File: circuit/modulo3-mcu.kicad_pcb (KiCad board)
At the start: 2 copper layers, 87 x 52 mm, 49 parts, among them Q1 BS250, Q2 BS170, U1 74LVC2G32DC, U10 PWR_CONN, U11 FOOTSWITCH, U13 LM1117 3V3, U2 AVR64DA64, U3 SN74LVC1G17, U4 UPDI, U5 TOUCHSCREEN_240x320, U6 FV1_CONN, U7 DBG_UART, U8 AMPCTRL, Y1 32768Hz

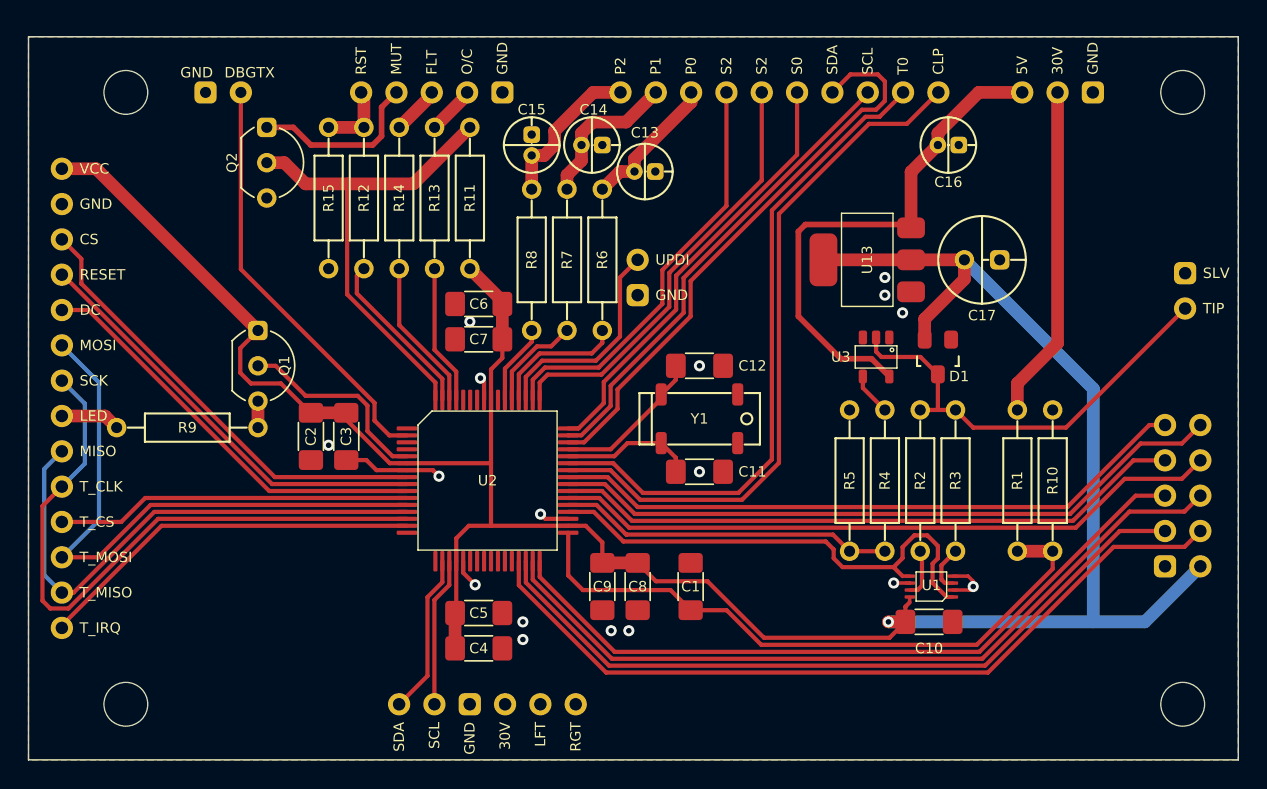
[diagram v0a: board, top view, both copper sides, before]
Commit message: added test pads for unused mcu pins
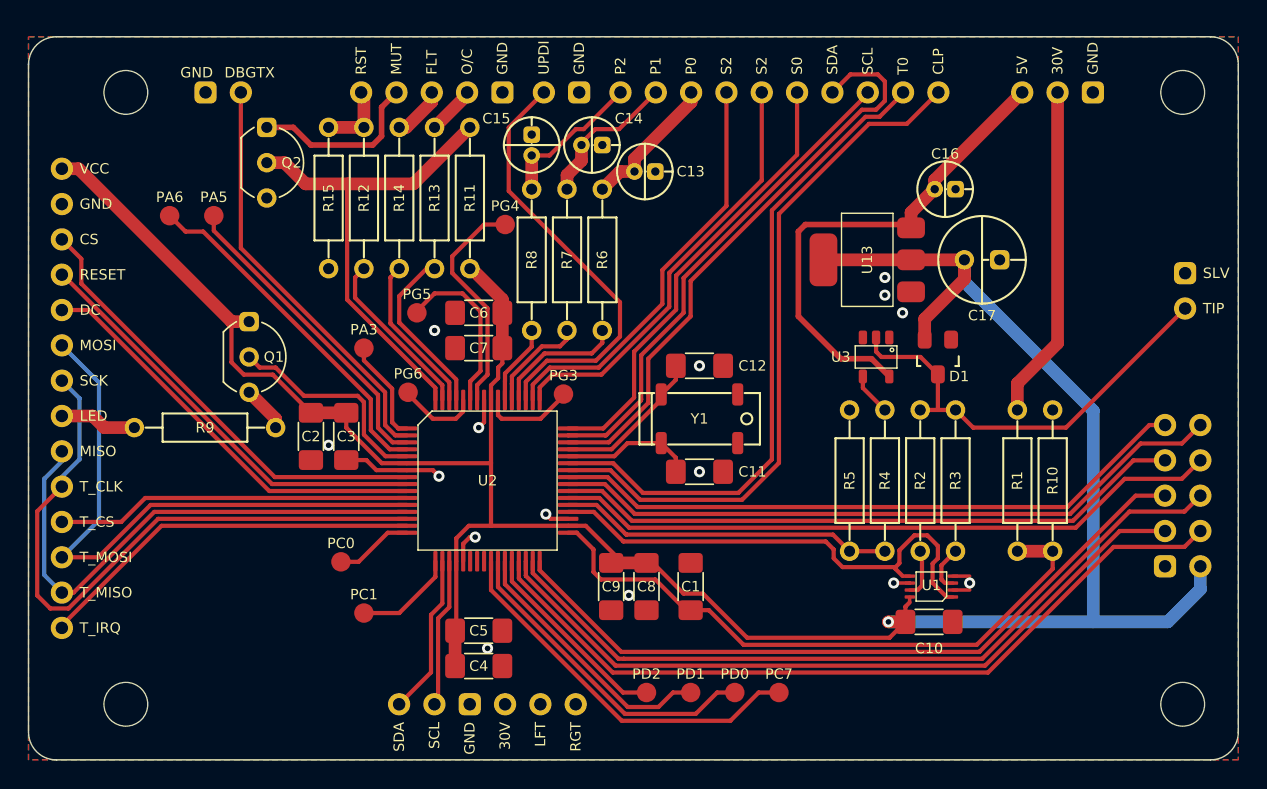
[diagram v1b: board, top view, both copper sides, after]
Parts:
- added T1: PA3, myAmp:TestPad, F.Cu at (71.1, 72.4)
- added T10: PD1, myAmp:TestPad, F.Cu at (94.6, 97.2)
- added T11: PD0, myAmp:TestPad, F.Cu at (97.8, 97.2)
- added T12: PC7, myAmp:TestPad, F.Cu at (101.0, 97.2)
- added T13: PG6, myAmp:TestPad, F.Cu at (74.3, 75.6)
- added T2: PD2, myAmp:TestPad, F.Cu at (91.4, 97.2)
- added T3: PA6, myAmp:TestPad, F.Cu at (57.1, 62.9)
- added T4: PC0, myAmp:TestPad, F.Cu at (69.5, 87.8)
- added T5: PC1, myAmp:TestPad, F.Cu at (71.1, 91.4)
- added T6: PG5, myAmp:TestPad, F.Cu at (74.9, 69.8)
- added T7: PG4, myAmp:TestPad, F.Cu at (81.3, 63.5)
- added T8: PG3, myAmp:TestPad, F.Cu at (85.5, 75.7)
- added T9: PA5, myAmp:TestPad, F.Cu at (60.3, 62.9)
- moved U4 15.2 mm to (86.6, 54.0), turned to 90 degrees
- moved C16 3.18 mm to (112.9, 61.0)
- moved C4 1.27 mm to (79.4, 95.2)
- moved C5 1.27 mm to (79.4, 92.7)
- moved R9 1.27 mm to (59.7, 78.1)
- moved Q1 0.90 mm to (62.9, 73.0)
- moved C7 0.64 mm to (79.4, 72.4)
- moved C9 0.64 mm to (88.9, 89.5)
- moved C6 0.63 mm to (79.4, 69.8)
- moved C8 0.63 mm to (91.4, 89.5)
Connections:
- U2 pad 1: unconnected-(U2-PA3-Pad1) -> Net-(U2-PA3)
- U2 pad 16: unconnected-(U2-PC0-Pad16) -> Net-(U2-PC0)
- U2 pad 17: unconnected-(U2-PC1-Pad17) -> Net-(U2-PC1)
- U2 pad 25: unconnected-(U2-PC7-Pad25) -> Net-(U2-PC7)
- U2 pad 26: unconnected-(U2-PD0-Pad26) -> Net-(U2-PD0)
- U2 pad 27: unconnected-(U2-PD1-Pad27) -> Net-(U2-PD1)
- U2 pad 28: unconnected-(U2-PD2-Pad28) -> Net-(U2-PD2)
- U2 pad 3: unconnected-(U2-PA5-Pad3) -> Net-(U2-PA5)
- U2 pad 4: unconnected-(U2-PA6-Pad4) -> Net-(U2-PA6)
- U2 pad 55: unconnected-(U2-PG3-Pad55) -> Net-(U2-PG3)
- U2 pad 58: unconnected-(U2-PG4-Pad58) -> Net-(U2-PG4)
- U2 pad 59: unconnected-(U2-PG5-Pad59) -> Net-(U2-PG5)
- U2 pad 60: unconnected-(U2-PG6-Pad60) -> Net-(U2-PG6)
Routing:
- net Net-(U2-PC7): track 0.00 -> 27.5 mm
- net Net-(U2-PA6): track 0.00 -> 25.3 mm
- net Net-(U2-PD0): track 0.00 -> 23.3 mm
- net Net-(U2-PA5): track 0.00 -> 22.7 mm
- net Net-(U2-PD1): track 0.00 -> 19.1 mm
- net Net-(U2-PG4): track 0.00 -> 16.4 mm
- net /UPDI: track 15.7 -> 31.3 mm
- net Net-(U2-PD2): track 0.00 -> 14.4 mm
- net Net-(U2-PG5): track 0.00 -> 12.4 mm
- net Net-(U2-PA3): track 0.00 -> 7.42 mm
- net Net-(U2-PC1): track 0.00 -> 7.34 mm
- net Net-(U2-PG3): track 0.00 -> 6.72 mm
- net Net-(U2-PG6): track 0.00 -> 5.88 mm
- net Net-(U2-PC0): track 0.00 -> 5.61 mm
- net /OTW_CLIP: track 10.1 -> 12.5 mm
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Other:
- outline, holes or cut-outs redrawn

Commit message: ready to panelize
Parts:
- added T14: PC4, myAmp:TestPad, B.Cu at (81.9, 94.6)
- added T15: PC5, myAmp:TestPad, F.Cu at (81.3, 93.3)
- added T16: PC6, myAmp:TestPad, F.Cu at (83.8, 95.2)
- U11: footprint myAmp:FOOTSWITCH -> myAmp:EXT_JACK
- moved C4 1.91 mm to (77.5, 95.2)
- moved C5 1.91 mm to (77.5, 92.7)
- moved T8 0.57 mm to (85.7, 76.2)
- moved U11 0.31 mm to (130.2, 67.3)
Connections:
- U2 pad 22: unconnected-(U2-PC4-Pad22) -> Net-(U2-PC4)
- U2 pad 23: unconnected-(U2-PC5-Pad23) -> Net-(U2-PC5)
- U2 pad 24: unconnected-(U2-PC6-Pad24) -> Net-(U2-PC6)
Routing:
- net GND: track 16.7 -> 26.0 mm
- net Net-(U2-PC6): track 0.00 -> 9.22 mm
- net Net-(U2-PC4): track 0.00 -> 8.22 mm, vias 0 -> 1
- net Net-(U2-PC5): track 0.00 -> 6.47 mm
- net /MIX_SCL: track 10.7 -> 12.4 mm
- net +3.3V: track 184.1 -> 184.9 mm
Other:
- board text added: "2023/03/19"
- board text added: "modulo3-mcu"

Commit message: attempt to send to fab: part II
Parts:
- U12: moved to B.Cu
- moved T3 15.8 mm to (67.7, 74.7)
- moved T9 11.6 mm to (67.7, 71.9)
- moved U11 4.45 mm to (130.2, 62.9)
- moved U12 0.50 mm to (129.5, 83.2), turned to -90 degrees
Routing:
- net Net-(U2-PA6): track 25.3 -> 9.90 mm
- net Net-(U2-PA5): track 22.7 -> 10.9 mm
- net Net-(U11-TIP): track 31.8 -> 36.0 mm
- net /ADC2: track 49.0 -> 48.5 mm
- net /RE_SW: track 56.3 -> 55.7 mm
- net /ADC0: track 48.4 -> 47.8 mm
- net /RE_LED: track 57.3 -> 56.7 mm
- net /RE_B: track 52.7 -> 52.2 mm
- net /ADC1: track 45.6 -> 45.1 mm
- net /ADC3: track 46.3 -> 45.7 mm
- net /RE_A: track 53.7 -> 53.2 mm
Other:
- board text added: "2023/04/16"
- board text removed: "2023/03/19"

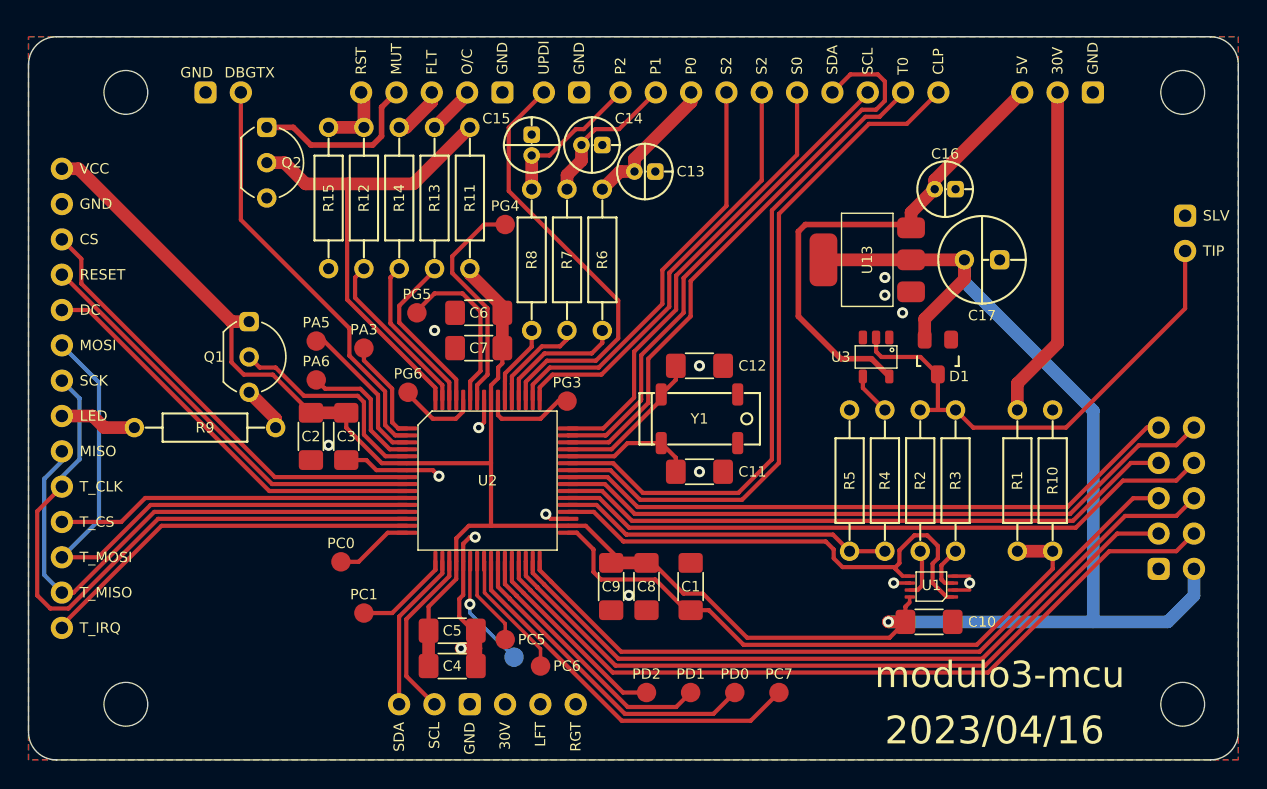
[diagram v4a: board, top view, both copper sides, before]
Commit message: fixed p mosfet for screen LED; started src
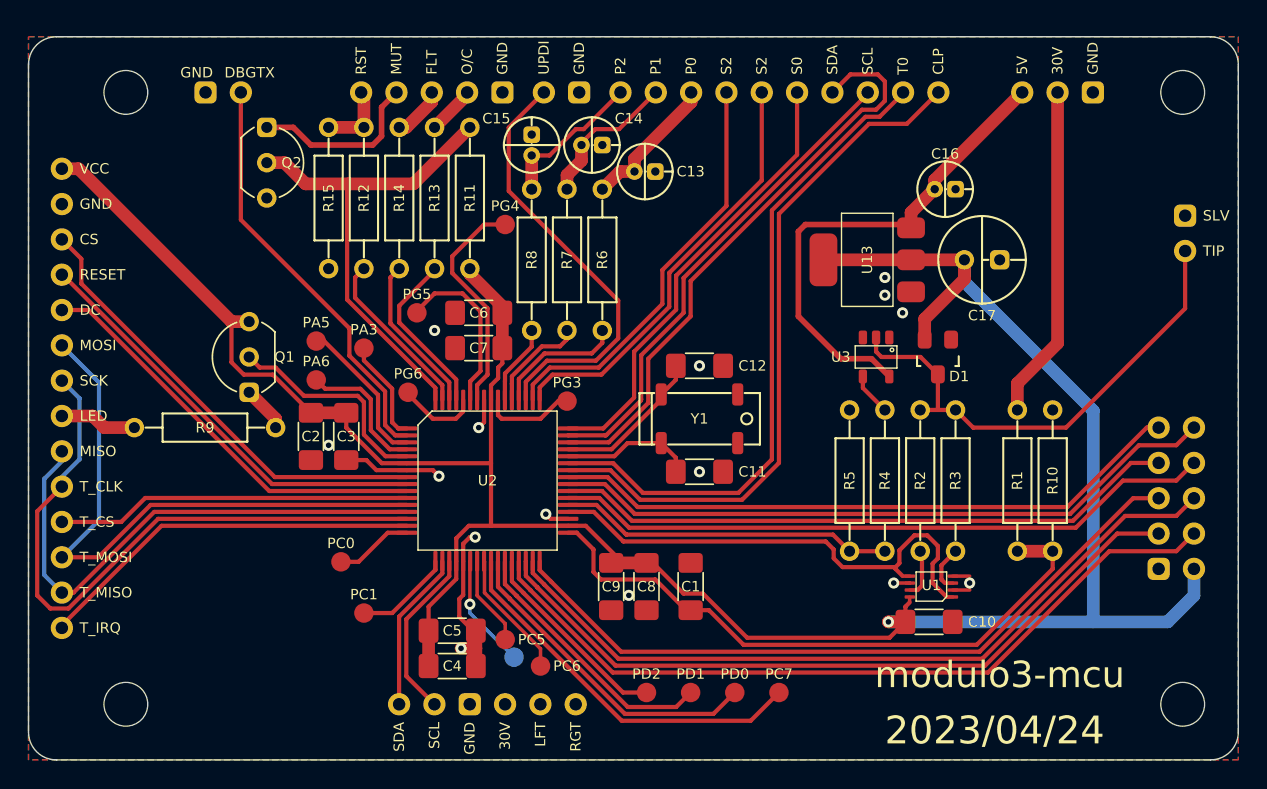
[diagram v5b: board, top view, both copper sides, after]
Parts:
- turned Q1 to 90 degrees
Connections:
- Q1 pad 1: +3.3V -> Net-(Q1-D)
- Q1 pad 3: Net-(Q1-S) -> +3.3V
- R9 pad 2: Net-(Q1-S) -> Net-(Q1-D)
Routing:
- net Net-(Q1-S): track 3.33 -> 0.00 mm
- net Net-(Q1-D): track 0.00 -> 3.33 mm
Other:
- board text added: "2023/04/24"
- board text removed: "2023/04/16"
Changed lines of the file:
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@@
   (net 3 "Net-(U2-(XTAL32K1)PF0)")
   (net 4 "Net-(U2-(XTAL32K2)PF1)")
-  (net 5 "Net-(Q1-S)")
+  (net 5 "Net-(Q1-D)")
   (net 6 "Net-(R2-Pad1)")
   (net 7 "Net-(R3-Pad1)")
@@
   )
   (footprint "myAmp:TO-92_Inline_Wide" (layer "F.Cu")
-    (at 62.865 73.025 -90)
+    (at 62.865 73.025 90)
     (descr "TO-92 leads in-line, wide, drill 0.8mm (see NXP sot054_po.pdf)")
     (tags "to-92 sc-43 sc-43a sot54 PA33 transistor")
@@
     (property "Sheetname" "")
     (attr through_hole)
-    (fp_text reference "Q1" (at 0 2.54 -180) (layer "F.SilkS")
+    (fp_text reference "Q1" (at 0 2.54) (layer "F.SilkS")
         (effects (font (size 0.75 0.75) (thickness 0.15)))
     )
@@
     (fp_arc (start 2.4892 0.9144) (mid 2.183093 1.410556) (end 1.8 1.85)
       (stroke (width 0.12) (type solid)) (layer "F.SilkS"))
-    (pad "1" thru_hole roundrect (at -2.54 0) (size 1.4 1.4) (drill 0.8) (layers "*.Cu" "*.Mask") (roundrect_rratio 0.25)
-      (net 2 "+3.3V") (pinfunction "D") (pintype "passive"))
-    (pad "2" thru_hole circle (at 0 0) (size 1.4 1.4) (drill 0.8) (layers "*.Cu" "*.Mask")
+    (pad "1" thru_hole roundrect (at -2.54 0 180) (size 1.4 1.4) (drill 0.8) (layers "*.Cu" "*.Mask") (roundrect_rratio 0.25)
+      (net 5 "Net-(Q1-D)") (pinfunction "D") (pintype "passive"))
+    (pad "2" thru_hole circle (at 0 0 180) (size 1.4 1.4) (drill 0.8) (layers "*.Cu" "*.Mask")
       (net 22 "/S_LED") (pinfunction "G") (pintype "input"))
-    (pad "3" thru_hole circle (at 2.54 0) (size 1.4 1.4) (drill 0.8) (layers "*.Cu" "*.Mask")
-      (net 5 "Net-(Q1-S)") (pinfunction "S") (pintype "passive"))
+    (pad "3" thru_hole circle (at 2.54 0 180) (size 1.4 1.4) (drill 0.8) (layers "*.Cu" "*.Mask")
+      (net 2 "+3.3V") (pinfunction "S") (pintype "passive"))
     (model "${KIPRJMOD}/myAmp.pretty/models/TO-92_Inline_Wide.step"
       (offset (xyz -2.54 0 0))
@@
       (net 14 "Net-(U5-LED)") (pintype "passive"))
     (pad "2" thru_hole circle (at 5.08 0) (size 1.4 1.4) (drill 0.8) (layers "*.Cu" "*.Mask")
-      (net 5 "Net-(Q1-S)") (pintype "passive"))
+      (net 5 "Net-(Q1-D)") (pintype "passive"))
     (model "${KIPRJMOD}/myAmp.pretty/models/R_Axial_DIN0207_L6.3mm_D2.5mm_P10.16mm_Horizontal.step"
       (offset (xyz -5.08 0 0))
@@
     (effects (font (size 1.9 1.9) (thickness 0.3)))
   )
-  (gr_text "2023/04/16" (at 116.475 99.885) (layer "F.SilkS")
+  (gr_text "2023/04/24" (at 116.475 99.885) (layer "F.SilkS")
     (effects (font (size 2 2) (thickness 0.3)))
   )

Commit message: lowered the watch resolution to .24 ms; moved the pins of the display; added pull-ups for mix i2c
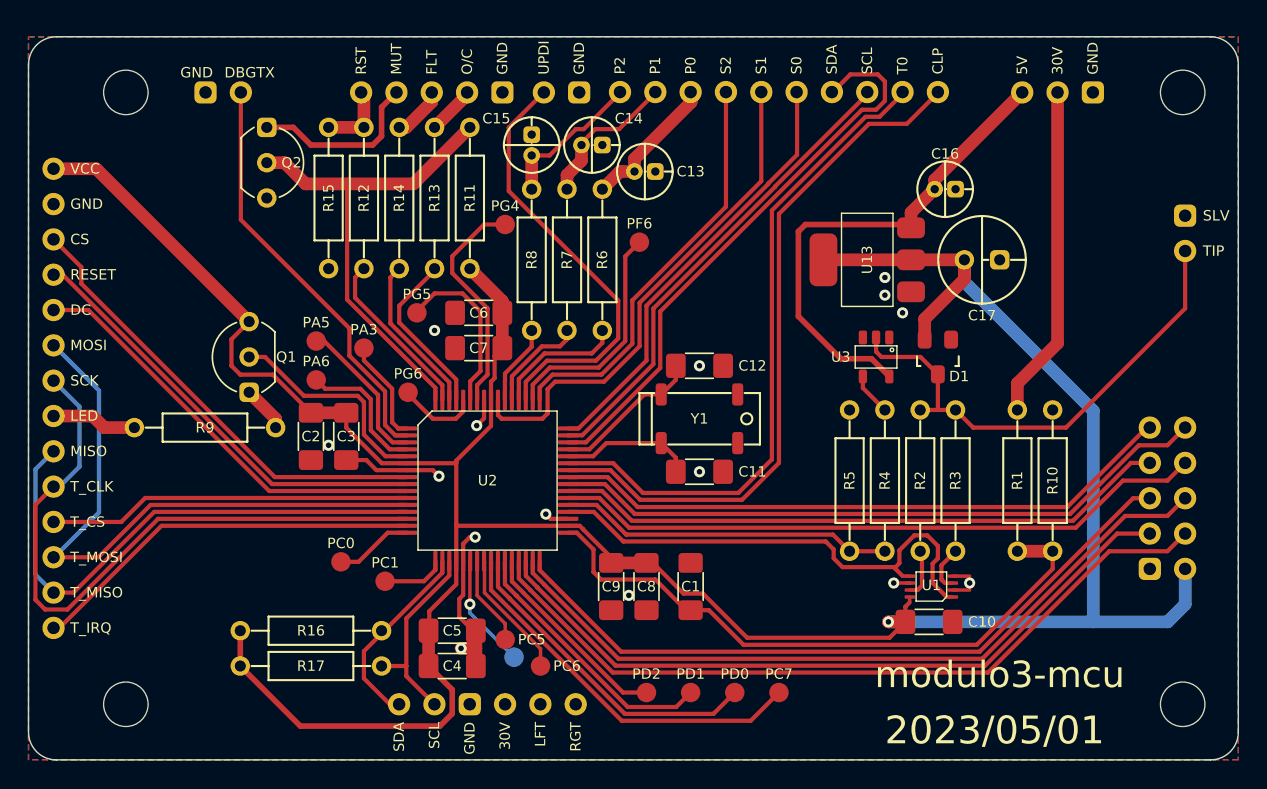
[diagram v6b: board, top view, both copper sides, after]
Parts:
- added R16: 4k7, myAmp:R_10MM, F.Cu at (67.3, 92.7)
- added R17: 4k7, myAmp:R_10MM, F.Cu at (67.3, 95.2)
- T8: value PG3 -> PF6
- moved T8 12.6 mm to (90.9, 64.8)
- moved T5 2.75 mm to (72.6, 89.2)
- moved U12 0.63 mm to (128.9, 83.2)
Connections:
- T8 pad 1: Net-(U2-PG3) -> Net-(U2-(~{RESET})PF6)
- U2 pad 49: /S1 -> /S2
- U2 pad 50: /S2 -> Net-(U2-(~{RESET})PF6)
- U2 pad 55: Net-(U2-PG3) -> /S1
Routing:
- net +3.3V: track 184.5 -> 208.1 mm
- net Net-(U2-(~{RESET})PF6): track 0.00 -> 16.6 mm
- net Net-(U2-PG3): track 6.69 -> 0.00 mm
- net /S1: track 30.8 -> 36.5 mm
- net /MIX_SDA: track 11.6 -> 14.1 mm
- net Net-(U2-PC1): track 7.04 -> 4.57 mm
- net /MIX_SCL: track 12.4 -> 14.2 mm
- net /S_MOSI: track 43.8 -> 45.0 mm
- net /S0: track 32.5 -> 31.4 mm
- net /FV_SCL: track 35.2 -> 34.2 mm
- net /FV_SDA: track 42.2 -> 41.2 mm
- net /S_SCK: track 46.9 -> 47.8 mm
- net /ADC3: track 45.7 -> 45.1 mm
- net /RE_B: track 52.2 -> 51.5 mm
- net /RE_A: track 53.2 -> 52.5 mm
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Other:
- board text added: "2023/05/01"
- board text removed: "2023/04/24"
